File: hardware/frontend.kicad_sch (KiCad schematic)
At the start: 83 parts, among them IC201 FMMT458TA, Q201 2N7002, U201 BQ769x2

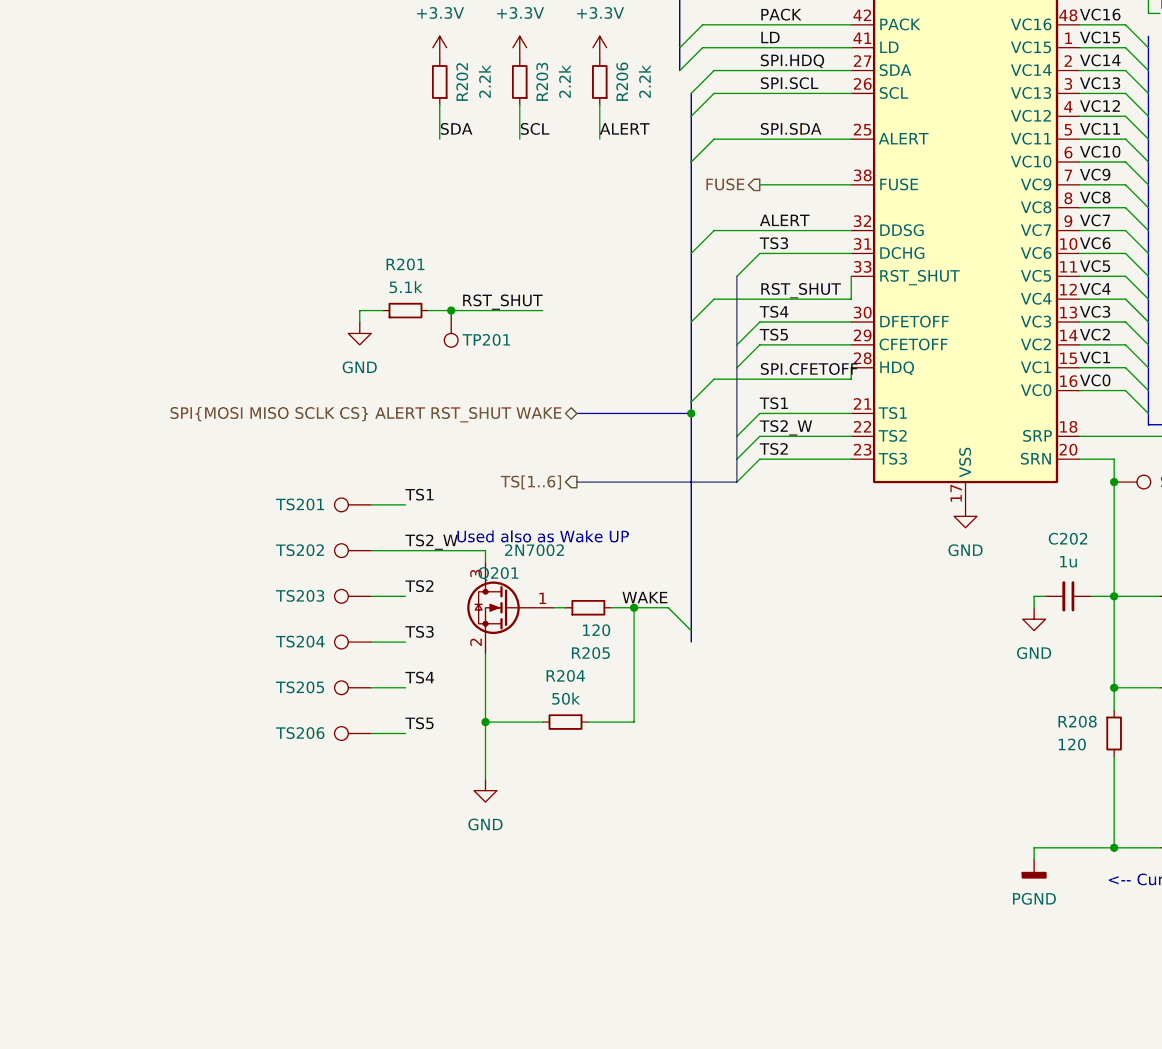
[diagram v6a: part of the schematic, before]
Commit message: change add thermoprotection
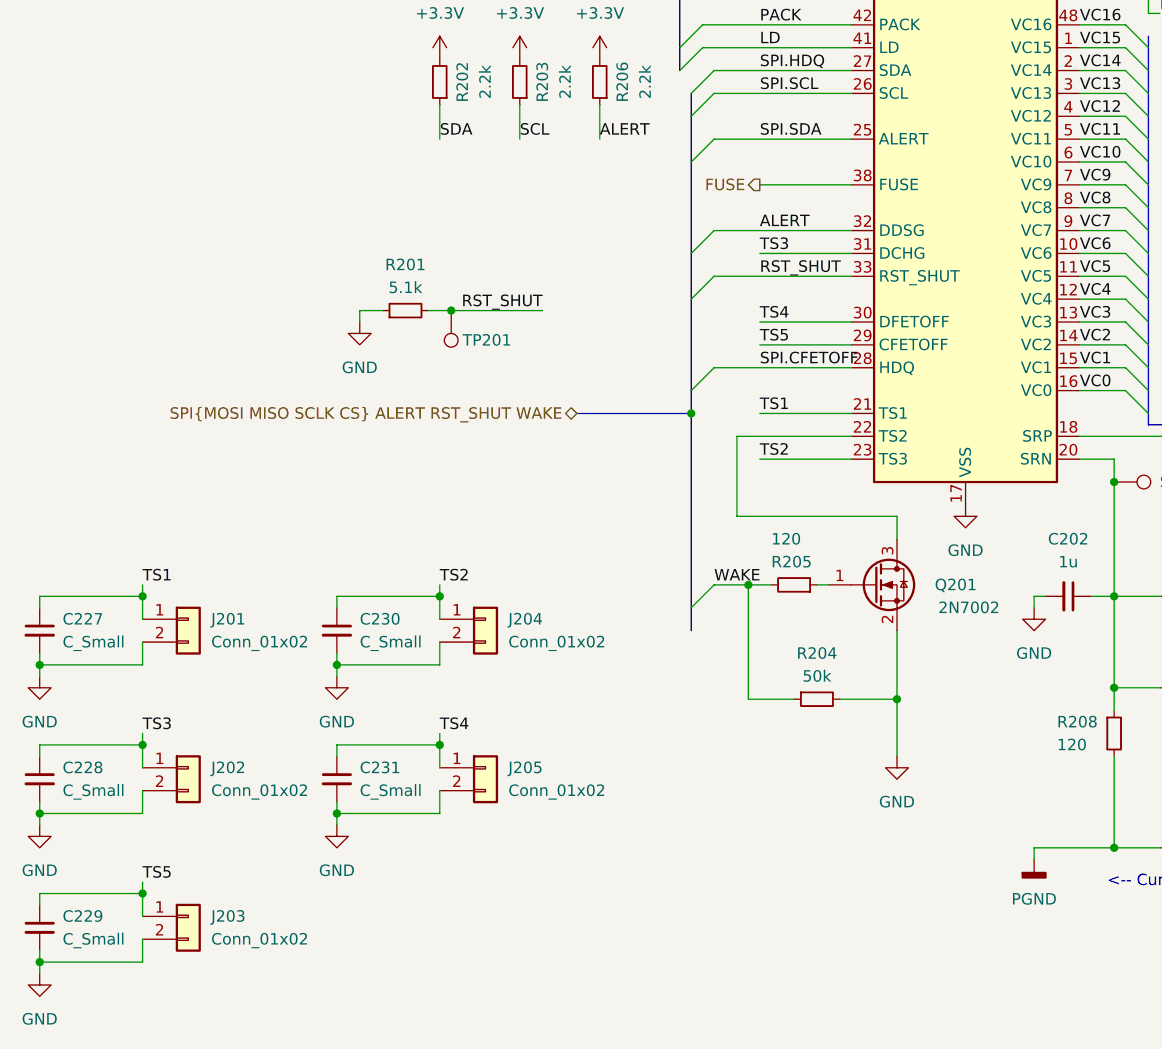
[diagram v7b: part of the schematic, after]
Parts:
- removed TS201, TS202, TS203, TS204, TS205, TS206: TestPoint, TestPoint:TestPoint_Pad_D1.0mm, symbol Connector:TestPoint
- added C227, C228, C229, C230, C231: C_Small, symbol Device:C_Small
- added J201, J202, J203, J204, J205: Conn_01x02, symbol Connector_Generic:Conn_01x02
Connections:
- net GND: now also C227.2, C228.2, C229.2, C230.2, C231.2, J201.2 (Pin_2), J202.2 (Pin_2), J203.2 (Pin_2), J204.2 (Pin_2), J205.2 (Pin_2)
- net TS1: now also C227.1, J201.1 (Pin_1)
- net TS2: now also C230.1, J204.1 (Pin_1)
- net TS3: now also C228.1, J202.1 (Pin_1)
- net TS4: now also C231.1, J205.1 (Pin_1)
- net TS5: now also C229.1, J203.1 (Pin_1)
- net TS2_W: no longer names the net of Q201.3 (D), U201.22 (TS2)
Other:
- note removed: "Used also as Wake UP"
- moved on the sheet: Q201, R204, R205

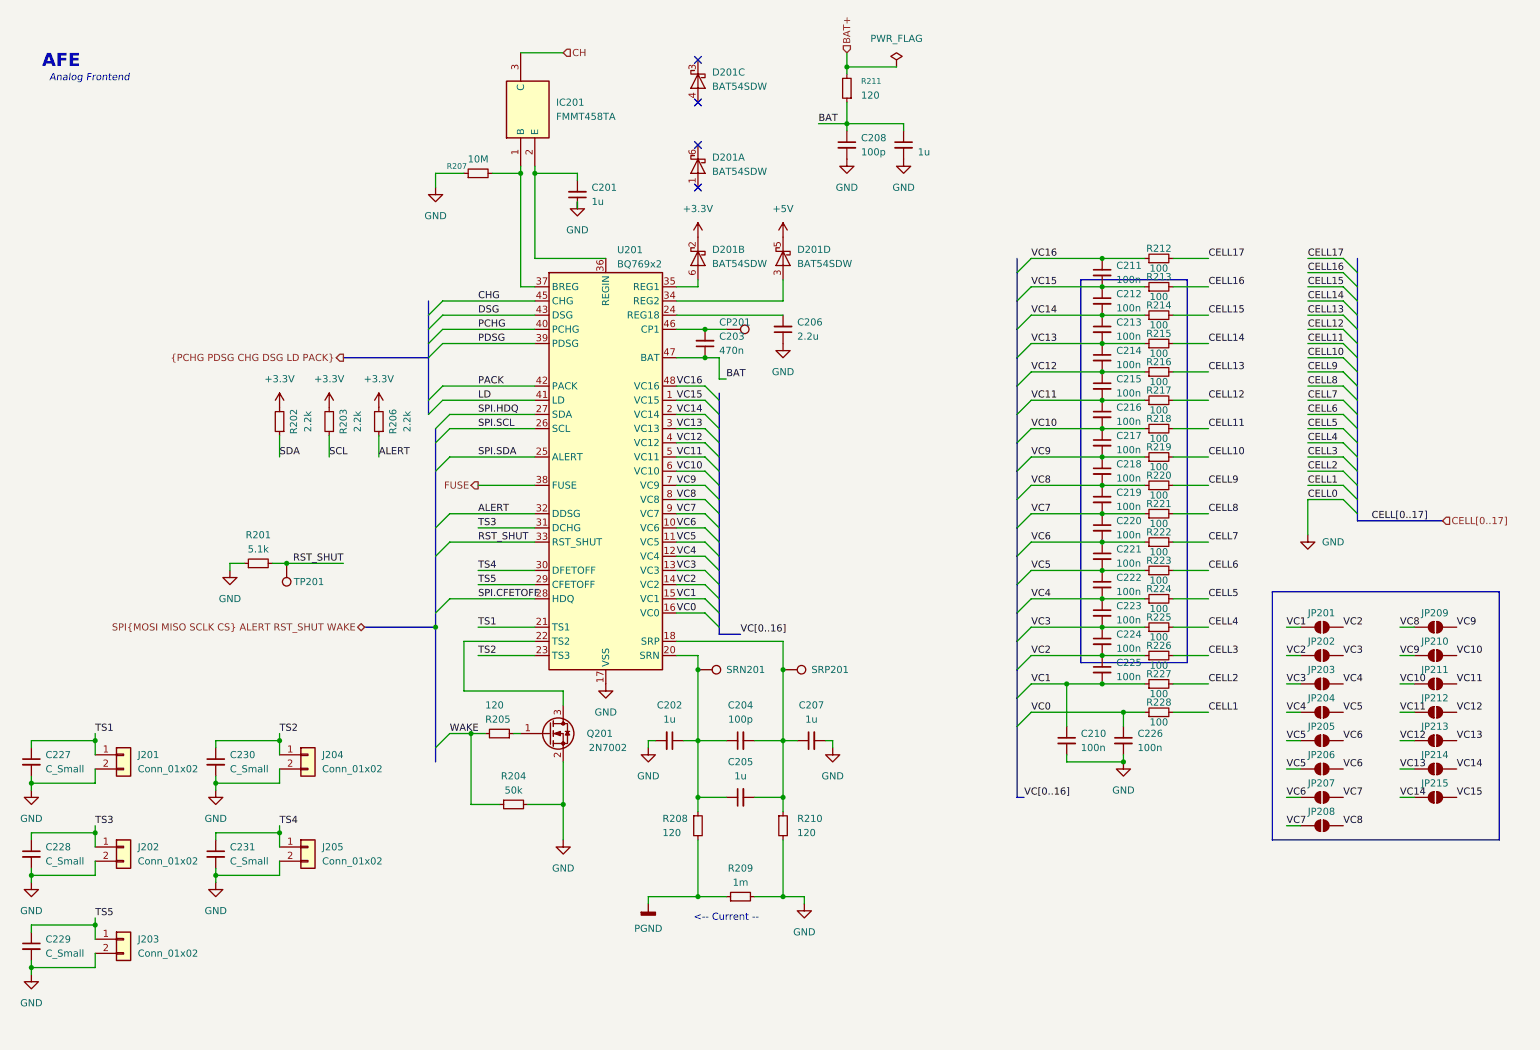
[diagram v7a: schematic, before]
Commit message: change add thermoprotection
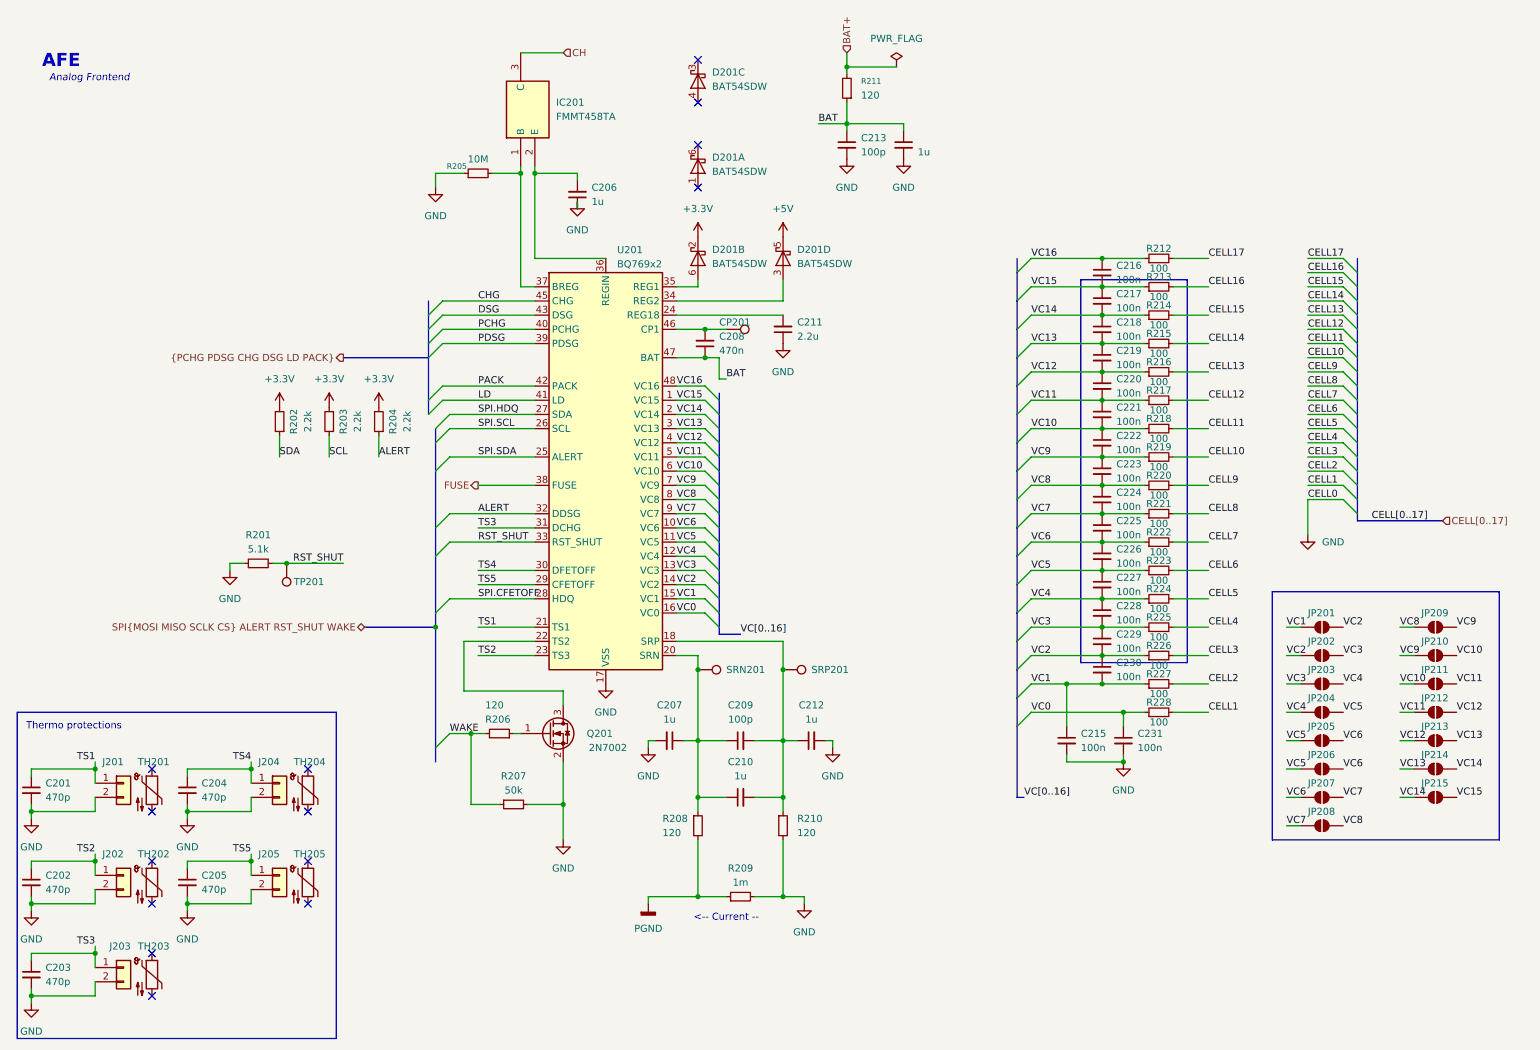
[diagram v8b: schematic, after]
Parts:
- added TH201, TH202, TH203, TH204, TH205: Thermistor_NTC, symbol Device:Thermistor_NTC
- C201: renamed from C227; value C_Small -> 470p
- C202: renamed from C228; value C_Small -> 470p
- C203: renamed from C229; value C_Small -> 470p
- C204: renamed from C230; value C_Small -> 470p
- C205: renamed from C231; value C_Small -> 470p
- renumbered C201 to C206, C202 to C207, C203 to C208, C204 to C209, C205 to C210, C206 to C211, C207 to C212, C208 to C213, C209 to C214, C210 to C215, C211 to C216, C212 to C217, C213 to C218, C214 to C219, C215 to C220, C216 to C221, C217 to C222, C218 to C223, C219 to C224, C220 to C225, C221 to C226, C222 to C227, C223 to C228, C224 to C229, C225 to C230, C226 to C231, R206 to R204, R207 to R205, R205 to R206, R204 to R207
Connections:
- net TS2: now also C202.1, J202.1 (Pin_1); no longer C204.1, J204.1 (Pin_1)
- net TS3: now also C203.1, J203.1 (Pin_1); no longer C202.1, J202.1 (Pin_1)
- net TS4: now also C204.1, J204.1 (Pin_1); no longer C205.1, J205.1 (Pin_1)
- net TS5: now also C205.1, J205.1 (Pin_1); no longer C203.1, J203.1 (Pin_1)
- no-connect marks 4 -> 14
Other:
- note added: "Thermo protections"
- moved on the sheet: C201, C202, C203, C204, C205, J201, J202, J203, J204, J205
